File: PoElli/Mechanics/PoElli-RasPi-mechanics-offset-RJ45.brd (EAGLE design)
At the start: 64 x 56 mm, 31 parts, among them J1 DF12-ELLI-HEADER-TOP, J2 M022.54MM, J3 M022.54MM, J4 M022.54MM, T1 Coilcraft 230NL, T2 FLYBACKEMBEDDED, U3 FST3257, X1 M-BOLT-2, X2 M-BOLT-2, X3 M-BOLT-2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

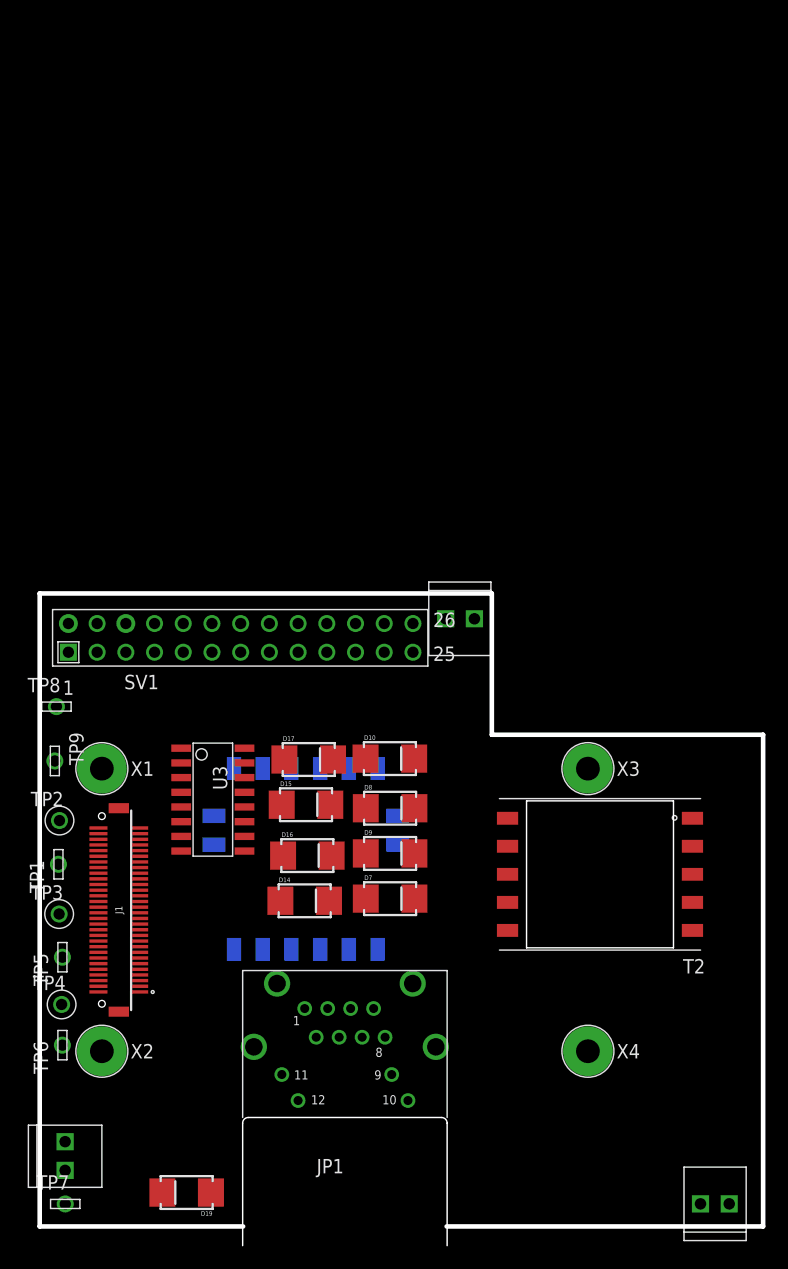
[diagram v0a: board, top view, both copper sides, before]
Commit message: Changes to PoElli-RasPi-offset-RJ45 from today's meeting
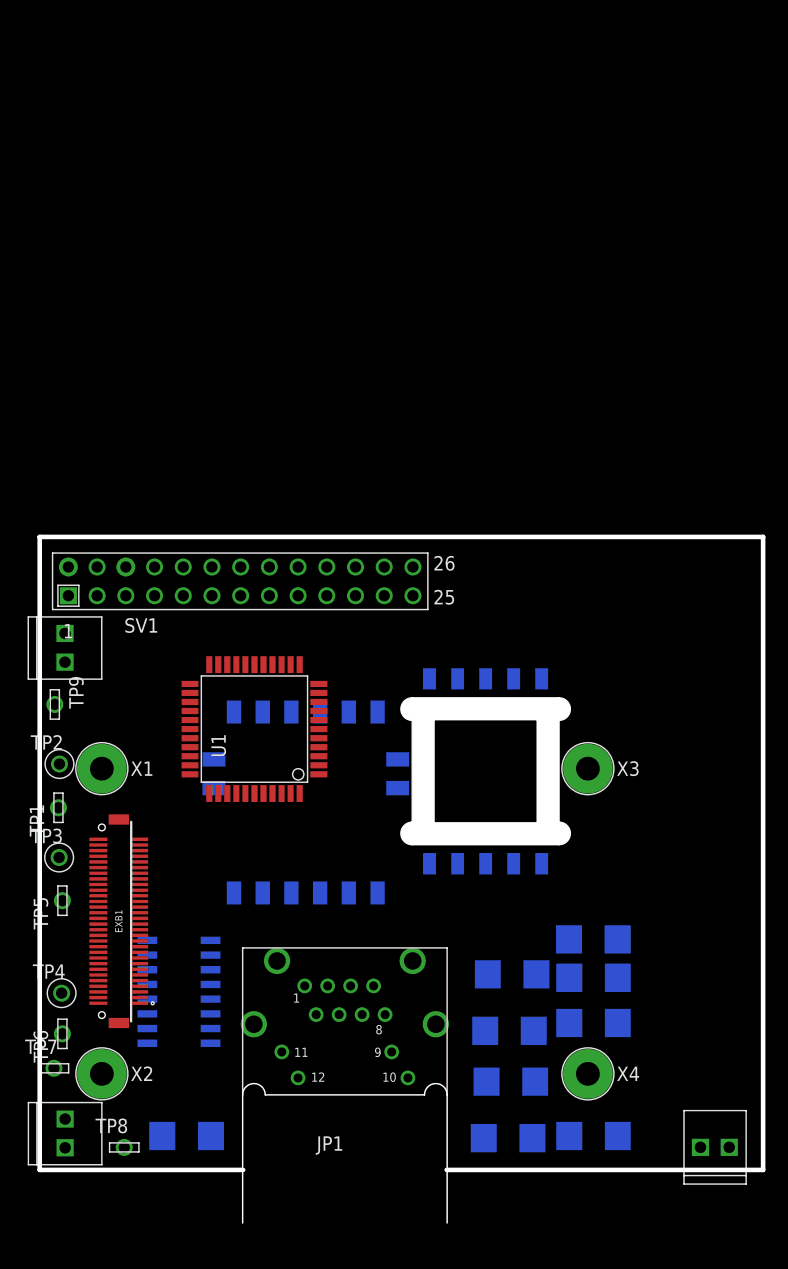
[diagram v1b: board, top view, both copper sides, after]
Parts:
- removed J1: DF12-ELLI-HEADER-TOP, ELL-i-Connectors:DF12(4.0)-60DP-0.5V
- added EXB1: DF12-ELLI-HEADER-TOP, ELL-i-Connectors:DF12(4.0)-60DP-0.5V
- added U1: ENC424J600, ELL-i-DigitalIC:TQFP44-0.8MM
- moved TP8 39.5 mm to (7.48, 6.99)
- moved J3 33.9 mm to (2.24, 49.9), turned to 90 degrees
- moved D14 27.7 mm to (41.4, 7.81), flipped to the bottom
- moved D7 27.7 mm to (49.0, 8.00), flipped to the bottom
- moved D15 26.9 mm to (41.6, 17.3), flipped to the bottom
- moved D16 26.9 mm to (41.7, 12.8), flipped to the bottom
- moved D17 26.2 mm to (41.8, 22.3), flipped to the bottom
- moved D10 24.1 mm to (49.0, 25.4), flipped to the bottom
- moved D8 23.4 mm to (49.0, 22.0), flipped to the bottom
- moved D9 23.4 mm to (49.0, 18.0), flipped to the bottom
- moved U3 17.3 mm to (12.3, 20.8), flipped to the bottom
- moved T2 13.6 mm to (39.5, 40.3), flipped to the bottom, turned to 90 degrees
- moved TP7 12.0 mm to (1.26, 14.0)
- moved D19 5.00 mm to (13.0, 8.00), flipped to the bottom
- moved J2 5.00 mm to (61.0, 7.00)
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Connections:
- new net VCAP: U1.43
- new net VDD: U1.44
- new net VDDOSC: U1.4
- new net VDDPLL: U1.12
- new net VDDRX: U1.15
- new net VDDTX: U1.18
- new net VSS1: U1.33
- new net VSS2: U1.42
- new net VSSOSC: U1.1
- new net VSSPLL: U1.13
- new net VSSRX: U1.14
- new net VSSTX1: U1.19
- new net VSSTX2: U1.22
- net 3.3V: now also EXB1.6; no longer J1.6
- net 5V: now also EXB1.8; no longer J1.8
- net GND: now also EXB1.12, EXB1.14; no longer J1.12, J1.14
- net VBATT: now also EXB1.4; no longer J1.4
- net VCC(IO): now also EXB1.2; no longer J1.2
- net VIN: now also EXB1.10; no longer J1.10
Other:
- outline, holes or cut-outs redrawn

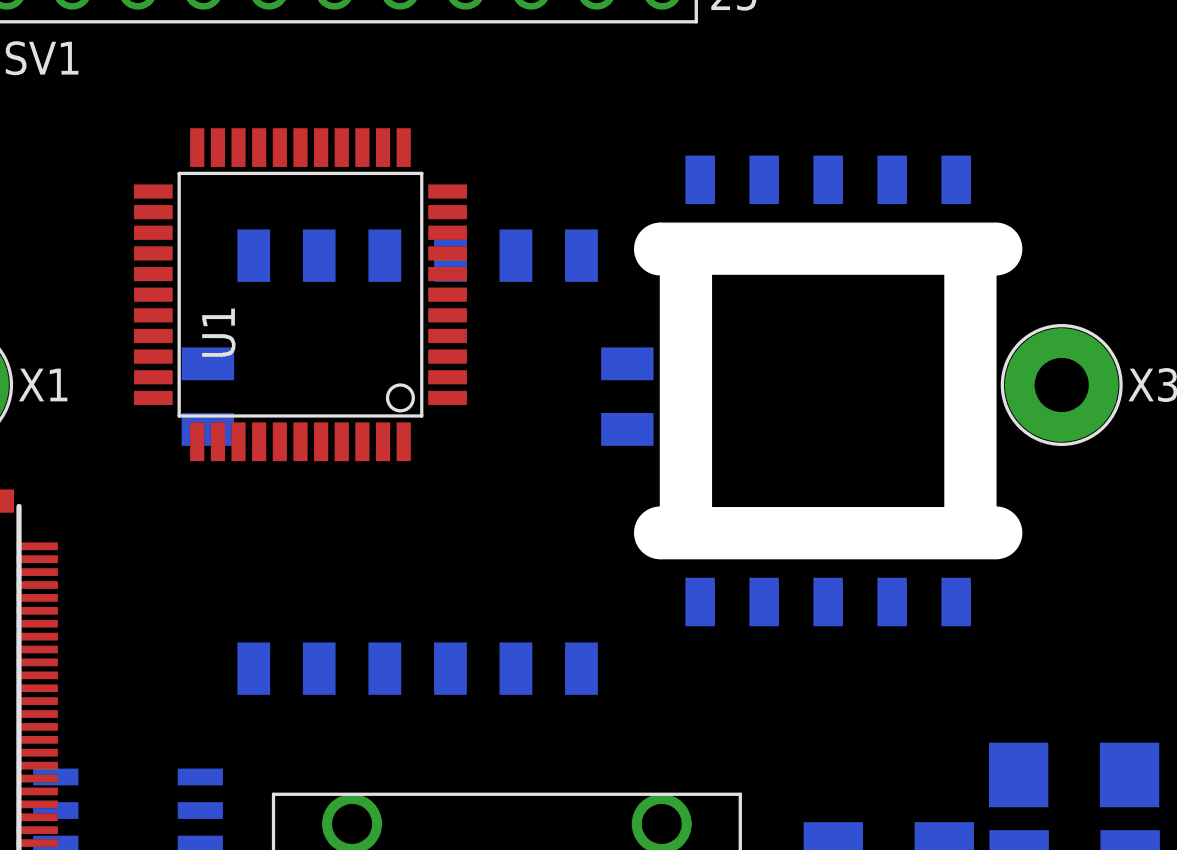
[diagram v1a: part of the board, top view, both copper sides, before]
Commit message: Move transformers in PoEll-i RasPi mechanics model
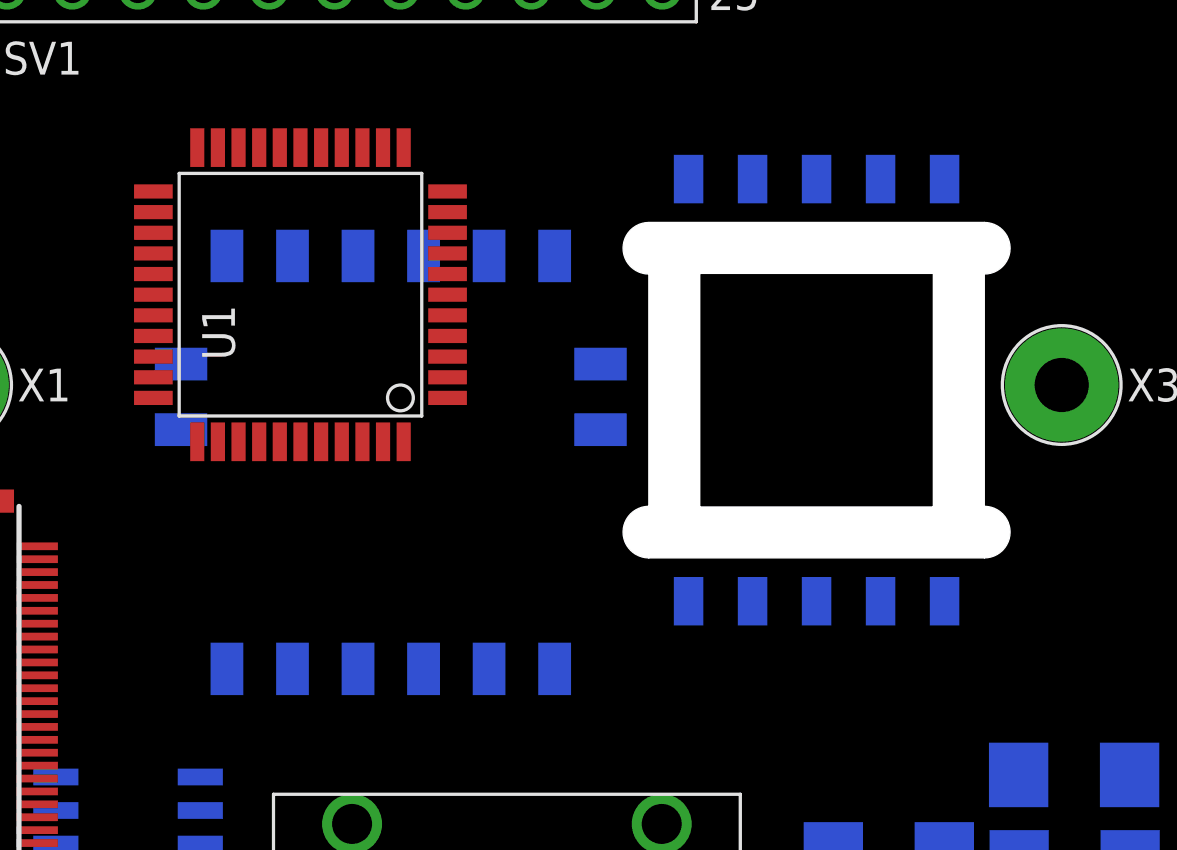
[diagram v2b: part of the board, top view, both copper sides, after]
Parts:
- moved T1 1.04 mm to (22.5, 37.5)
- moved T2 0.45 mm to (39.0, 40.3)
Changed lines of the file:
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@@
 </autorouter>
 <elements>
-<element name="T1" library="ELL-i-Transformers" package="COILCRAFT-ETH1-230L" value="Coilcraft 230NL" x="23.54" y="37.51" rot="MR180"/>
+<element name="T1" library="ELL-i-Transformers" package="COILCRAFT-ETH1-230L" value="Coilcraft 230NL" x="22.5" y="37.5" rot="MR180"/>
 <element name="SV1" library="ELL-i-Boards" package="RASPBERRYPI-SHIELD-CONNECTOR" value="RASPBERRY-SHIELDCONNECTOR" x="0" y="5" smashed="yes">
 <attribute name="NAME" x="10.54" y="53.8" size="1.27" layer="25" ratio="10" rot="R180"/>
@@
 <element name="D8" library="ELL-i-DIscreteSemi" package="DIODE-B2100" value="B2100" x="49" y="22" rot="MR0"/>
 <element name="D7" library="ELL-i-DIscreteSemi" package="DIODE-B2100" value="B2100" x="49" y="8" rot="MR0"/>
-<element name="T2" library="ELL-i-Transformers" package="WE_EP13_SMD_10PIN_EMBEDDED" value="FLYBACKEMBEDDED" x="39.45" y="40.27" rot="MR90"/>
+<element name="T2" library="ELL-i-Transformers" package="WE_EP13_SMD_10PIN_EMBEDDED" value="FLYBACKEMBEDDED" x="39" y="40.3" rot="MR90"/>
 <element name="J4" library="SparkFun-Connectors" package="1X02_2.54_SCREWTERM" value="M022.54MM" x="2.25" y="6.96" rot="R90"/>
 <element name="U3" library="ELL-i-DigitalIC" package="SOIC-16-NARROW" value="FST3257" x="12.32" y="20.76" rot="MR270"/>
@@
 <contactref element="T1" pad="10"/>
 <contactref element="JP1" pad="2"/>
-<wire x1="24.46" y1="18.74" x2="27.35" y2="45.511" width="0" layer="19" extent="16-16"/>
+<wire x1="24.46" y1="18.74" x2="26.31" y2="45.501" width="0" layer="19" extent="16-16"/>
 </signal>
 <signal name="N$2">
 <contactref element="T1" pad="9"/>
 <contactref element="JP1" pad="1"/>
-<wire x1="23.444" y1="21.28" x2="29.89" y2="45.511" width="0" layer="19" extent="16-16"/>
+<wire x1="23.444" y1="21.28" x2="28.85" y2="45.501" width="0" layer="19" extent="16-16"/>
 </signal>
 <signal name="N$3">
 <contactref element="T1" pad="13"/>
 <contactref element="JP1" pad="3"/>
-<wire x1="25.476" y1="21.28" x2="19.73" y2="45.511" width="0" layer="19" extent="16-16"/>
+<wire x1="25.476" y1="21.28" x2="18.69" y2="45.501" width="0" layer="19" extent="16-16"/>
 </signal>
 <signal name="N$4">
 <contactref element="T1" pad="14"/>
 <contactref element="JP1" pad="6"/>
-<wire x1="28.524" y1="18.74" x2="17.19" y2="45.511" width="0" layer="19" extent="16-16"/>
+<wire x1="28.524" y1="18.74" x2="16.15" y2="45.501" width="0" layer="19" extent="16-16"/>
 </signal>
 <signal name="POE_B-">
@@
 <contactref element="T1" pad="12"/>
 <wire x1="39.41" y1="17.31" x2="51.15" y2="22" width="0" layer="19" extent="1-1"/>
-<wire x1="22.27" y1="45.511" x2="39.41" y2="17.31" width="0" layer="19" extent="1-16"/>
+<wire x1="21.23" y1="45.501" x2="39.41" y2="17.31" width="0" layer="19" extent="1-16"/>
 </signal>
 <signal name="POE_B+">

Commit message: Update RasPi outline & connector
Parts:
- added OUTLINE1: RASPBERRY-OUTLINE, ELL-i-Boards:RASPBERRYPI-SHIELD-OUTLINE
- SV1: value RASPBERRY-SHIELDCONNECTOR -> RASPBERRY-CONNECTOR
- moved SV1 55.0 mm to (17.8, 57.1)
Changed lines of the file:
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@@
 <layer number="47" name="Measures" color="7" fill="1" visible="no" active="yes"/>
 <layer number="48" name="Document" color="7" fill="1" visible="yes" active="yes"/>
-<layer number="49" name="Reference" color="7" fill="1" visible="no" active="yes"/>
+<layer number="49" name="Reference" color="7" fill="1" visible="yes" active="yes"/>
 <layer number="50" name="dxf" color="7" fill="1" visible="no" active="no"/>
 <layer number="51" name="tDocu" color="7" fill="1" visible="yes" active="yes"/>
@@
 <layer number="111" name="111" color="7" fill="1" visible="no" active="yes"/>
 <layer number="112" name="tSilk" color="7" fill="1" visible="no" active="yes"/>
+<layer number="113" name="IDFDebug" color="4" fill="1" visible="yes" active="yes"/>
 <layer number="116" name="Patch_BOT" color="9" fill="4" visible="no" active="yes"/>
 <layer number="118" name="Rect_Pads" color="7" fill="1" visible="no" active="yes"/>
@@
 <elements>
 <element name="T1" library="ELL-i-Transformers" package="COILCRAFT-ETH1-230L" value="Coilcraft 230NL" x="22.5" y="37.5" rot="MR180"/>
-<element name="SV1" library="ELL-i-Boards" package="RASPBERRYPI-SHIELD-CONNECTOR" value="RASPBERRY-SHIELDCONNECTOR" x="0" y="5" smashed="yes">
-<attribute name="NAME" x="10.54" y="53.8" size="1.27" layer="25" ratio="10" rot="R180"/>
-<attribute name="VALUE" x="34.04" y="53.8" size="1.27" layer="27" ratio="10" rot="R180"/>
+<element name="SV1" library="ELL-i-Boards" package="RASPBERRYPI-SHIELD-CONNECTOR" value="RASPBERRY-CONNECTOR" x="17.78" y="57.07" smashed="yes">
+<attribute name="NAME" x="28.32" y="105.87" size="1.27" layer="25" ratio="10" rot="R180"/>
+<attribute name="VALUE" x="51.82" y="105.87" size="1.27" layer="27" ratio="10" rot="R180"/>
 </element>
 <element name="EXB1" library="ELL-i-Connectors" package="DF12(4.0)-60DP-0.5V" value="DF12-ELLI-HEADER-TOP" x="7" y="27" rot="R90"/>
@@
 <element name="J2" library="SparkFun-Connectors" package="1X02_2.54_SCREWTERM" value="M022.54MM" x="61" y="7" rot="R180"/>
 <element name="U1" library="ELL-i-DigitalIC" package="TQFP44-0.8MM" value="ENC424J600" x="19" y="44" rot="R90"/>
+<element name="OUTLINE1" library="ELL-i-Boards" package="RASPBERRYPI-SHIELD-OUTLINE" value="RASPBERRY-OUTLINE" x="0" y="5"/>
 </elements>
 <signals>
@@
 <contactref element="SV1" pad="4"/>
 <contactref element="SV1" pad="2"/>
+<wire x1="5.08" y1="58.34" x2="5.1999" y2="21.25" width="0" layer="19" extent="1-1"/>
 <wire x1="2.54" y1="58.34" x2="5.08" y2="58.34" width="0" layer="19" extent="1-1"/>
-<wire x1="5.1999" y1="21.25" x2="5.08" y2="58.34" width="0" layer="19" extent="1-1"/>
 </signal>
 <signal name="POE_A+">
@@
 <contactref element="SV1" pad="14"/>
 <contactref element="SV1" pad="6"/>
-<wire x1="25.4" y1="58.34" x2="33.02" y2="55.8" width="0" layer="19" extent="1-1"/>
+<wire x1="5.1999" y1="22.25" x2="15.12" y2="16.21" width="0" layer="19" extent="1-16"/>
+<wire x1="5.1999" y1="22.75" x2="5.1999" y2="22.25" width="0" layer="19" extent="1-1"/>
+<wire x1="25.4" y1="58.34" x2="15.12" y2="16.21" width="0" layer="19" extent="16-16"/>
 <wire x1="17.78" y1="58.34" x2="25.4" y2="58.34" width="0" layer="19" extent="1-1"/>
 <wire x1="12.7" y1="55.8" x2="17.78" y2="58.34" width="0" layer="19" extent="1-1"/>
 <wire x1="7.62" y1="58.34" x2="12.7" y2="55.8" width="0" layer="19" extent="1-1"/>
-<wire x1="15.12" y1="16.21" x2="12.7" y2="55.8" width="0" layer="19" extent="1-1"/>
-<wire x1="5.1999" y1="22.75" x2="15.12" y2="16.21" width="0" layer="19" extent="1-1"/>
-<wire x1="5.1999" y1="22.25" x2="5.1999" y2="22.75" width="0" layer="19" extent="1-1"/>
+<wire x1="33.02" y1="55.8" x2="25.4" y2="58.34" width="0" layer="19" extent="1-1"/>
 </signal>
 <signal name="3.3V">
@@
 <contactref element="SV1" pad="1"/>
 <contactref element="SV1" pad="17"/>
+<wire x1="22.86" y1="55.8" x2="5.1999" y2="20.75" width="0" layer="19" extent="1-1"/>
 <wire x1="2.54" y1="55.8" x2="22.86" y2="55.8" width="0" layer="19" extent="1-1"/>
-<wire x1="5.1999" y1="20.75" x2="2.54" y2="55.8" width="0" layer="19" extent="1-1"/>
 </signal>
 <signal name="VCC">
